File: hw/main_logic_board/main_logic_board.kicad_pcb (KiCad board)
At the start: 2 copper layers, 8 parts, among them J1 BATT_IN, J2 PWR_SEL, U1 PocketBeagle, U2 MPU-9250, U3 BME280

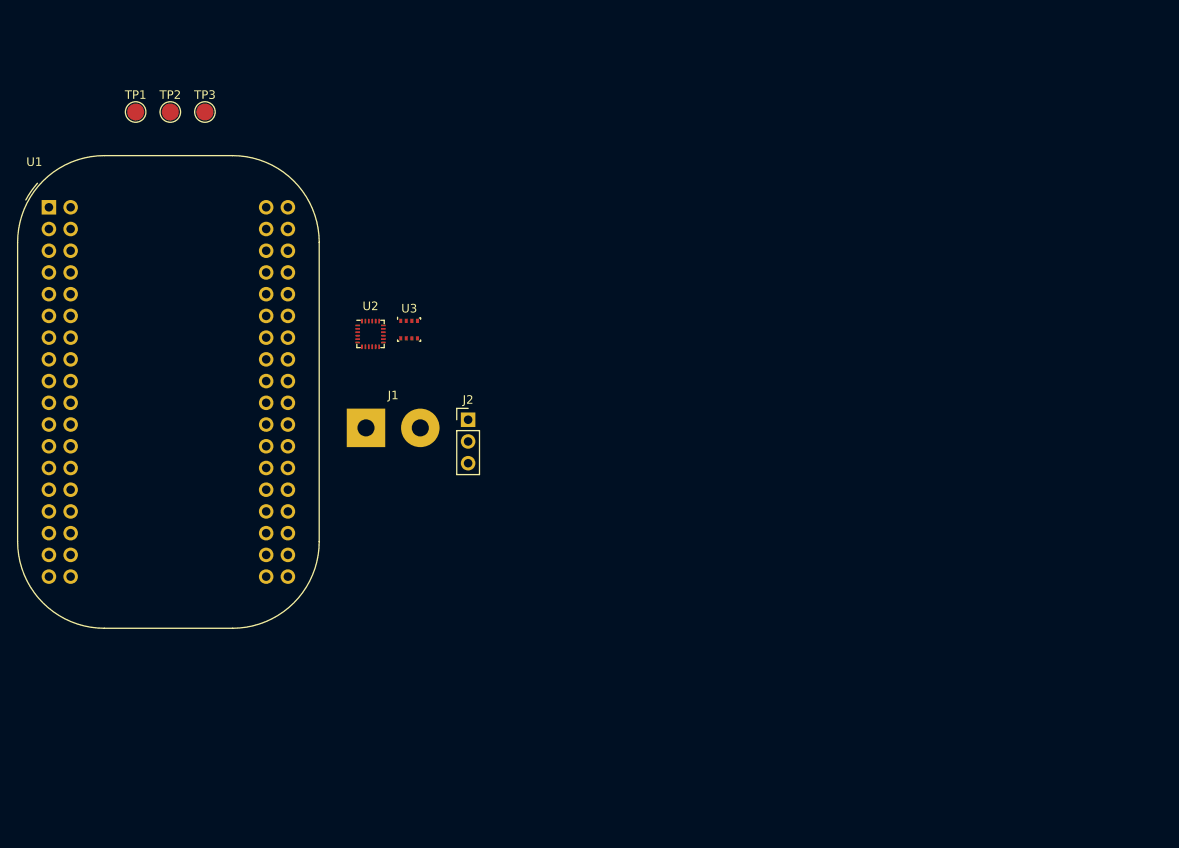
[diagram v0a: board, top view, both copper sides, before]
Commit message: Finish initial power schematics, swap some footprints for visualization in pcb view
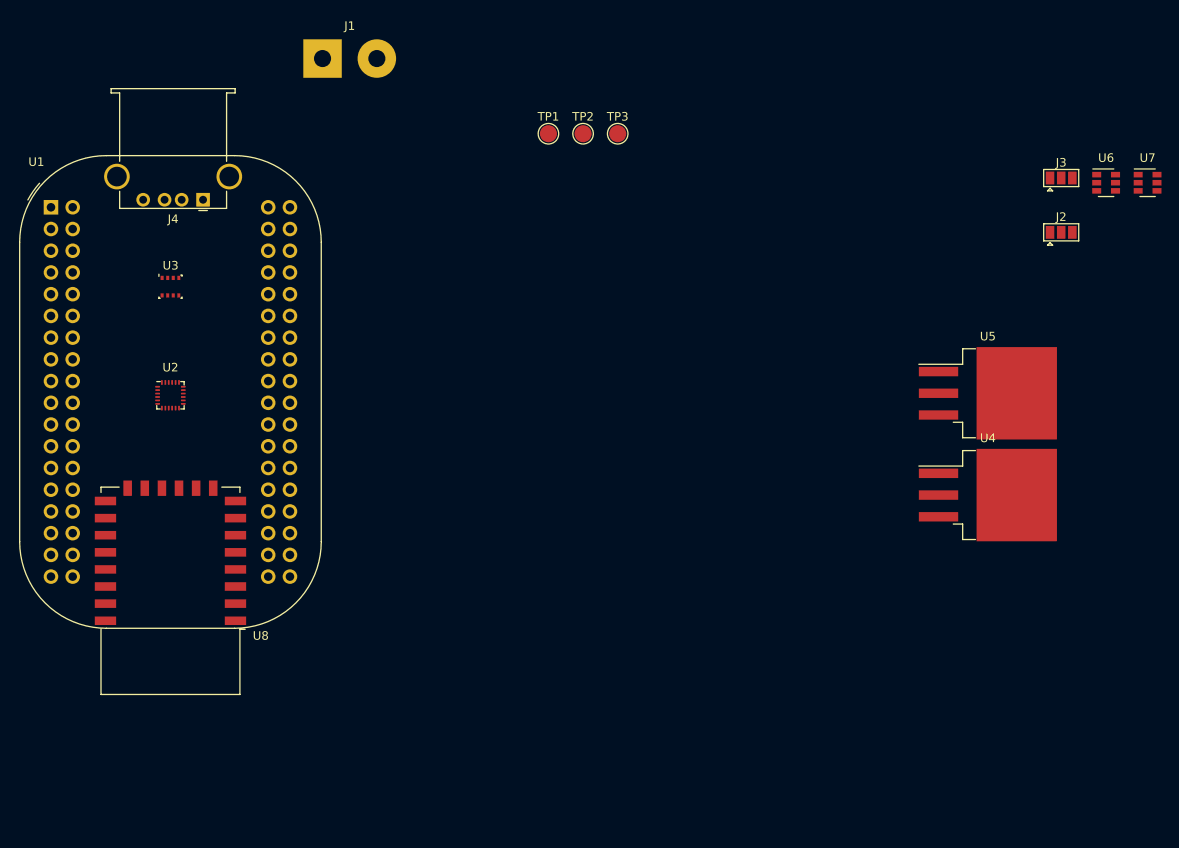
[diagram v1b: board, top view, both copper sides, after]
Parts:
- added J3: 3V3_PWR_SEL, Jumper:SolderJumper-3_P1.3mm_Open_Pad1.0x1.5mm, F.Cu at (221.0, 58.4)
- added J4: USB_A, Connector_USB:USB_A_Stewart_SS-52100-001_Horizontal, F.Cu at (120.7, 61.0)
- added U4: LM1085-5.0, Package_TO_SOT_SMD:TO-263-3_TabPin2, F.Cu at (212.4, 95.5)
- added U5: LM1085-3.3, Package_TO_SOT_SMD:TO-263-3_TabPin2, F.Cu at (212.4, 83.6)
- added U6: TPS563200, Package_TO_SOT_SMD:SOT-23-6, F.Cu at (226.2, 59.0)
- added U7: TPS563200, Package_TO_SOT_SMD:SOT-23-6, F.Cu at (231.1, 59.0)
- added U8: ESP-12F, RF_Module:ESP-12E, F.Cu at (116.8, 106.7)
- J2: value PWR_SEL -> 5V_PWR_SEL; footprint Connector_PinHeader_2.54mm:PinHeader_1x03_P2.54mm_Vertical -> Jumper:SolderJumper-3_P1.3mm_Open_Pad1.0x1.5mm
- moved J2 72.7 mm to (221.0, 64.8)
- moved TP2 48.3 mm to (165.1, 53.2)
- moved TP1 48.3 mm to (161.0, 53.2)
- moved TP3 48.3 mm to (169.1, 53.2)
- moved J1 43.5 mm to (134.6, 44.5)
- moved U3 28.3 mm to (116.8, 71.1)
- moved U2 24.5 mm to (116.8, 83.8)
- moved U1 0.24 mm to (102.9, 61.8)
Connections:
- net /RC_OUT_1 renamed /RC_OUT_5
- net Net-(U1-Pad19) renamed /AIN_1V8
- net Net-(U1-Pad20) renamed /GPIO20
- net Net-(U1-Pad34) renamed /GPIO26
- net Net-(U1-Pad36) renamed /PWM0
- net Net-(U1-Pad37) renamed /PWM1
- net Net-(U1-Pad39) renamed /GPIO23
- net Net-(U1-Pad55) renamed /GPIO27
- net Net-(U1-Pad64) renamed /RC_OUT_6
- net Net-(U1-Pad70) renamed /RC_OUT_4
- net Net-(U1-Pad71) renamed /AIN_3V3
- net Net-(U3-Pad4) renamed /SPI1_SCLK
- J1 pad 2: Net-(J1-Pad2) -> Net-(F1-Pad2)
- J2 pad 2: Net-(J1-Pad2) -> Net-(F1-Pad1)
- U1 pad 31: /RC_OUT_3 -> /RC_OUT_2
- U1 pad 33: /RC_OUT_0 -> /RC_OUT_3
- U1 pad 66: /RC_OUT_2 -> /SPI1_CS1
- U1 pad 67: /SPI1_CS -> /SPI1_CS0
- U2 pad 1: Net-(U2-Pad1) -> +3V3
- U2 pad 11: Net-(U2-Pad11) -> GND
- U2 pad 13: Net-(U2-Pad13) -> +3V3
- U2 pad 18: Net-(U2-Pad18) -> GND
- U2 pad 20: Net-(U2-Pad20) -> GND
- U2 pad 22: Net-(U2-Pad22) -> /SPI1_CS1
- U2 pad 23: Net-(U2-Pad23) -> /SPI1_CLK
- U2 pad 24: Net-(U2-Pad24) -> /SPI1_MOSI
- U2 pad 8: Net-(U2-Pad8) -> +3V3
- U2 pad 9: Net-(U2-Pad9) -> /SPI1_MISO
- U3 pad 1: Net-(U3-Pad1) -> GND
- U3 pad 2: Net-(U3-Pad2) -> /SPI1_CS0
- U3 pad 3: Net-(U3-Pad3) -> /SPI1_MOSI
- U3 pad 5: Net-(U3-Pad5) -> /SPI1_MISO
- U3 pad 6: Net-(U3-Pad6) -> +3V3
- U3 pad 7: Net-(U3-Pad7) -> GND
- U3 pad 8: Net-(U3-Pad8) -> +3V3

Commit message: Finish prelim schematic + PCB component placement
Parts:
- added C1: 47uF, Capacitor_SMD:C_0805_2012Metric, B.Cu at (142.4, 75.7)
- added C10: 10u, Capacitor_SMD:C_0805_2012Metric, B.Cu at (155.3, 98.4)
- added C11: 10u, Capacitor_SMD:C_0805_2012Metric, B.Cu at (155.3, 103.5)
- added C12: 10u, Capacitor_SMD:C_0805_2012Metric, B.Cu at (153.1, 98.4)
- added C13: 100n, Capacitor_SMD:C_0805_2012Metric, B.Cu at (154.6, 92.1)
- added C14: 100n, Capacitor_SMD:C_0805_2012Metric, B.Cu at (155.6, 109.3)
- added C15: 22u, Capacitor_SMD:C_0805_2012Metric, B.Cu at (166.6, 95.8)
- added C16: 22u, Capacitor_SMD:C_0805_2012Metric, B.Cu at (166.1, 105.8)
- added C17: 22u, Capacitor_SMD:C_0805_2012Metric, B.Cu at (168.8, 95.8)
- added C18: 22u, Capacitor_SMD:C_0805_2012Metric, B.Cu at (168.3, 105.8)
- added C19: 22u, Capacitor_SMD:C_0805_2012Metric, B.Cu at (170.6, 105.8)
- added C2: 10u, Capacitor_SMD:C_0805_2012Metric, B.Cu at (129.6, 96.7)
- added C20: 100n, Capacitor_SMD:C_0805_2012Metric, F.Cu at (151.8, 95.7)
- added C21: 100n, Capacitor_SMD:C_0805_2012Metric, F.Cu at (144.8, 95.7)
- added C22: 100n, Capacitor_SMD:C_0805_2012Metric, B.Cu at (152.3, 74.1)
- added C23: 10uF, Capacitor_SMD:C_0805_2012Metric, F.Cu at (143.8, 121.2)
- added C3: 10u, Capacitor_SMD:C_0805_2012Metric, B.Cu at (140.8, 93.9)
- added C4: 100n, Capacitor_SMD:C_0805_2012Metric, F.Cu at (151.8, 103.5)
- added C5: 100n, Capacitor_SMD:C_0805_2012Metric, F.Cu at (145.6, 88.2)
- added C6: 100n, Capacitor_SMD:C_0805_2012Metric, F.Cu at (145.1, 103.6)
- added C7: 10u, Capacitor_SMD:C_0805_2012Metric, B.Cu at (129.6, 102.9)
- added C8: 10u, Capacitor_SMD:C_0805_2012Metric, B.Cu at (140.8, 106.0)
- added C9: 10u, Capacitor_SMD:C_0805_2012Metric, B.Cu at (153.1, 103.5)
- added D1: WS2813, LED_SMD:LED_WS2812_PLCC6_5.0x5.0mm_P1.6mm, B.Cu at (135.1, 130.3)
- added D2: WS2813, LED_SMD:LED_WS2812_PLCC6_5.0x5.0mm_P1.6mm, B.Cu at (161.4, 130.3)
- added D3: WS2813, LED_SMD:LED_WS2812_PLCC6_5.0x5.0mm_P1.6mm, B.Cu at (161.2, 70.0)
- added D4: WS2813, LED_SMD:LED_WS2812_PLCC6_5.0x5.0mm_P1.6mm, B.Cu at (135.2, 70.0)
- added D5: RED, Diode_SMD:D_0805_2012Metric, F.Cu at (150.8, 130.6)
- added H1: GND, MountingHole:MountingHole_2.2mm_M2_Pad_Via, F.Cu at (126.6, 81.7)
- added H10: PWR, MountingHole:MountingHole_2.2mm_M2_Pad_Via, F.Cu at (174.3, 111.5)
- added H11: SIG, MountingHole:MountingHole_2.2mm_M2_Pad_Via, F.Cu at (174.0, 116.3)
- added H12: GND, MountingHole:MountingHole_2.2mm_M2_Pad_Via, F.Cu at (169.8, 118.7)
- added H2: SIG, MountingHole:MountingHole_2.2mm_M2_Pad_Via, F.Cu at (122.4, 84.1)
- added H3: PWR, MountingHole:MountingHole_2.2mm_M2_Pad_Via, F.Cu at (122.1, 88.9)
- added H4: PWR, MountingHole:MountingHole_2.2mm_M2_Pad_Via, F.Cu at (122.1, 111.5)
- added H5: SIG, MountingHole:MountingHole_2.2mm_M2_Pad_Via, F.Cu at (122.4, 116.3)
- added H6: GND, MountingHole:MountingHole_2.2mm_M2_Pad_Via, F.Cu at (126.6, 118.7)
- added H7: GND, MountingHole:MountingHole_2.2mm_M2_Pad_Via, F.Cu at (169.8, 81.7)
- added H8: SIG, MountingHole:MountingHole_2.2mm_M2_Pad_Via, F.Cu at (174.0, 84.1)
- added H9: PWR, MountingHole:MountingHole_2.2mm_M2_Pad_Via, F.Cu at (174.3, 88.9)
- added J10: RC_OUT_6, Connector_PinHeader_1.27mm:PinHeader_1x03_P1.27mm_Vertical, F.Cu at (150.0, 114.4)
- added J5: RC_OUT_1, Connector_PinHeader_1.27mm:PinHeader_1x03_P1.27mm_Vertical, F.Cu at (136.9, 75.5)
- added J6: RC_OUT_2, Connector_PinHeader_1.27mm:PinHeader_1x03_P1.27mm_Vertical, F.Cu at (134.3, 124.8)
- added J7: RC_OUT_3, Connector_PinHeader_1.27mm:PinHeader_1x03_P1.27mm_Vertical, F.Cu at (160.1, 75.5)
- added J8: RC_OUT_4, Connector_PinHeader_1.27mm:PinHeader_1x03_P1.27mm_Vertical, F.Cu at (160.0, 124.8)
- added J9: RC_OUT_5, Connector_PinHeader_1.27mm:PinHeader_1x03_P1.27mm_Vertical, F.Cu at (147.0, 114.4)
- added L1: 3.3u 20mOhm, Inductor_SMD:L_Abracon_ASPI-0630LR, B.Cu at (160.9, 90.3)
- added L2: 2.2u 15mOhm, Inductor_SMD:L_Vishay_IHLP-2020, B.Cu at (161.1, 110.5)
- added R1: 56.2k, Resistor_SMD:R_0805_2012Metric, B.Cu at (166.8, 90.3)
- added R10: 10K, Resistor_SMD:R_0805_2012Metric, F.Cu at (141.9, 126.8)
- added R2: 10k, Resistor_SMD:R_0805_2012Metric, B.Cu at (163.1, 96.0)
- added R3: 33.2k, Resistor_SMD:R_0805_2012Metric, B.Cu at (166.1, 110.7)
- added R4: 10k, Resistor_SMD:R_0805_2012Metric, B.Cu at (162.6, 105.5)
- added R5: 0R, Resistor_SMD:R_0805_2012Metric, F.Cu at (153.1, 74.3)
- added R6: 10K, Resistor_SMD:R_0805_2012Metric, F.Cu at (144.6, 131.3)
- added R7: 1K, Resistor_SMD:R_0805_2012Metric, F.Cu at (152.0, 125.6)
- added R8: 10K, Resistor_SMD:R_0805_2012Metric, F.Cu at (152.0, 123.4)
- added R9: 10K, Resistor_SMD:R_0805_2012Metric, F.Cu at (152.0, 121.2)
- added SW1: ESP_RESET, Button_Switch_SMD:SW_SPST_B3U-1000P, F.Cu at (141.8, 130.5)
- added SW2: ESP_GPIO0, Button_Switch_SMD:SW_SPST_B3U-1000P, F.Cu at (155.2, 130.5)
- added TP4: AIN_VREF+, TestPoint:TestPoint_Pad_D1.0mm, F.Cu at (141.2, 99.0)
- added TP5: AIN_VREF-, TestPoint:TestPoint_Pad_D1.0mm, F.Cu at (141.1, 102.0)
- added U10: ICM-20948, Sensor_Motion:InvenSense_QFN-24_3x3mm_P0.4mm, F.Cu at (148.3, 95.7)
- added U11: VL53L1X, Sensor_Distance:ST_VL53L1x, B.Cu at (148.5, 74.2)
- added U9: USBLC6-2P6, lib:SOT50P160X60-6N, F.Cu at (148.4, 75.0)
- J1: footprint Connector_Wire:SolderWirePad_1x02_P7.62mm_Drill2mm -> Connector_Wire:SolderWirePad_1x02_P5.08mm_Drill1.5mm
- J2, J3, U6, U7, U8: moved to B.Cu
- TP1: value TP_5V -> TP_5V_VIN; footprint TestPoint:TestPoint_Pad_D2.0mm -> TestPoint:TestPoint_Pad_D1.0mm
- TP2: value TP_3V3 -> TP_3V3_PB; footprint TestPoint:TestPoint_Pad_D2.0mm -> TestPoint:TestPoint_Pad_D1.0mm
- TP3: footprint TestPoint:TestPoint_Pad_D2.0mm -> TestPoint:TestPoint_Pad_D1.0mm
- U1: footprint Module:BeagleBoard_PocketBeagle -> lib:BeagleBoard_PocketBeagle_SMD
- U4: value LM1085-5.0 -> NCP1117-5.0_SOT223; footprint Package_TO_SOT_SMD:TO-263-3_TabPin2 -> Package_TO_SOT_SMD:SOT-223-3_TabPin2; moved to B.Cu
- U5: value LM1085-3.3 -> NCP1117-3.3_SOT223; footprint Package_TO_SOT_SMD:TO-263-3_TabPin2 -> Package_TO_SOT_SMD:SOT-223-3_TabPin2; moved to B.Cu
- moved J2 103.8 mm to (125.8, 106.1), turned to 180 degrees
- moved J3 101.5 mm to (125.8, 93.7)
- moved U7 86.0 mm to (158.7, 105.3)
- moved U5 80.0 mm to (135.2, 104.2)
- moved U4 77.3 mm to (135.2, 95.7)
- moved U6 77.2 mm to (158.7, 96.2)
- moved TP3 60.2 mm to (141.2, 106.5)
- moved J1 58.6 mm to (125.7, 102.4), turned to 90 degrees
- moved TP2 54.2 mm to (155.7, 106.7)
- moved U8 39.3 mm to (148.5, 130.0), turned to 0 degrees
- moved U2 37.3 mm to (148.4, 103.5)
- moved TP1 36.3 mm to (141.3, 83.8)
- moved U3 35.9 mm to (148.4, 88.2)
- moved U1 35.8 mm to (134.5, 78.6)
- moved J4 32.7 mm to (151.9, 70.7)
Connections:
- net /AIN_1V8 renamed /AIN_1V8_0
- net Net-(F1-Pad1) renamed +BATT
- net Net-(U1-Pad21) renamed /AIN_1V8_1
- net Net-(U8-Pad10) renamed /telemetry/TELEM_MISO
- net Net-(U8-Pad13) renamed /telemetry/TELEM_MOSI
- net Net-(U8-Pad14) renamed /telemetry/TELEM_SCLK
- net Net-(U8-Pad9) renamed /telemetry/TELEM_CS_N
- J4 pad 4: Net-(J4-Pad4) -> GND
- J4 pad 5: Net-(J4-Pad5) -> GND
- TP2 pad 1: +3V3 -> /3V3_PB
- U1 pad 13: Net-(U1-Pad13) -> GND
- U1 pad 14: +3V3 -> /3V3_PB
- U1 pad 26: /I2C_SDA -> /I2C2_SDA
- U1 pad 28: /I2C_SCL -> /I2C2_SCL
- U1 pad 29: Net-(U1-Pad29) -> /RC_OUT_1
- U1 pad 45: Net-(U1-Pad45) -> /I2C1_SCL
- U1 pad 47: Net-(U1-Pad47) -> /I2C1_SDA
- U1 pad 5: Net-(U1-Pad5) -> +5V
- U1 pad 59: +3V3 -> /3V3_PB
- U2 pad 22: /SPI1_CS1 -> /sensors/MPU_CS_N
- U2 pad 23: /SPI1_CLK -> /I2C2_SCL
- U2 pad 24: /SPI1_MOSI -> /I2C2_SDA
- U2 pad 9: /SPI1_MISO -> /sensors/MPU_MISO
- U3 pad 2: /SPI1_CS0 -> /sensors/BME_CS_N
- U3 pad 3: /SPI1_MOSI -> /I2C2_SDA
- U3 pad 4: /SPI1_SCLK -> /I2C2_SCL
- U3 pad 5: /SPI1_MISO -> /sensors/BME_MISO
- U8 pad 1: Net-(U8-Pad1) -> /telemetry/RST_N
- U8 pad 15: Net-(U8-Pad15) -> GND
- U8 pad 16: Net-(U8-Pad16) -> /telemetry/GPIO15
- U8 pad 17: Net-(U8-Pad17) -> /telemetry/GPIO2
- U8 pad 18: Net-(U8-Pad18) -> /telemetry/GPIO0
- U8 pad 21: Net-(U8-Pad21) -> /UART4_TX
- U8 pad 22: Net-(U8-Pad22) -> /UART4_RX
- U8 pad 3: Net-(U8-Pad3) -> /telemetry/CH_PD
- U8 pad 8: Net-(U8-Pad8) -> +3V3
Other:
- board outline added: 61.9 x 69 mm

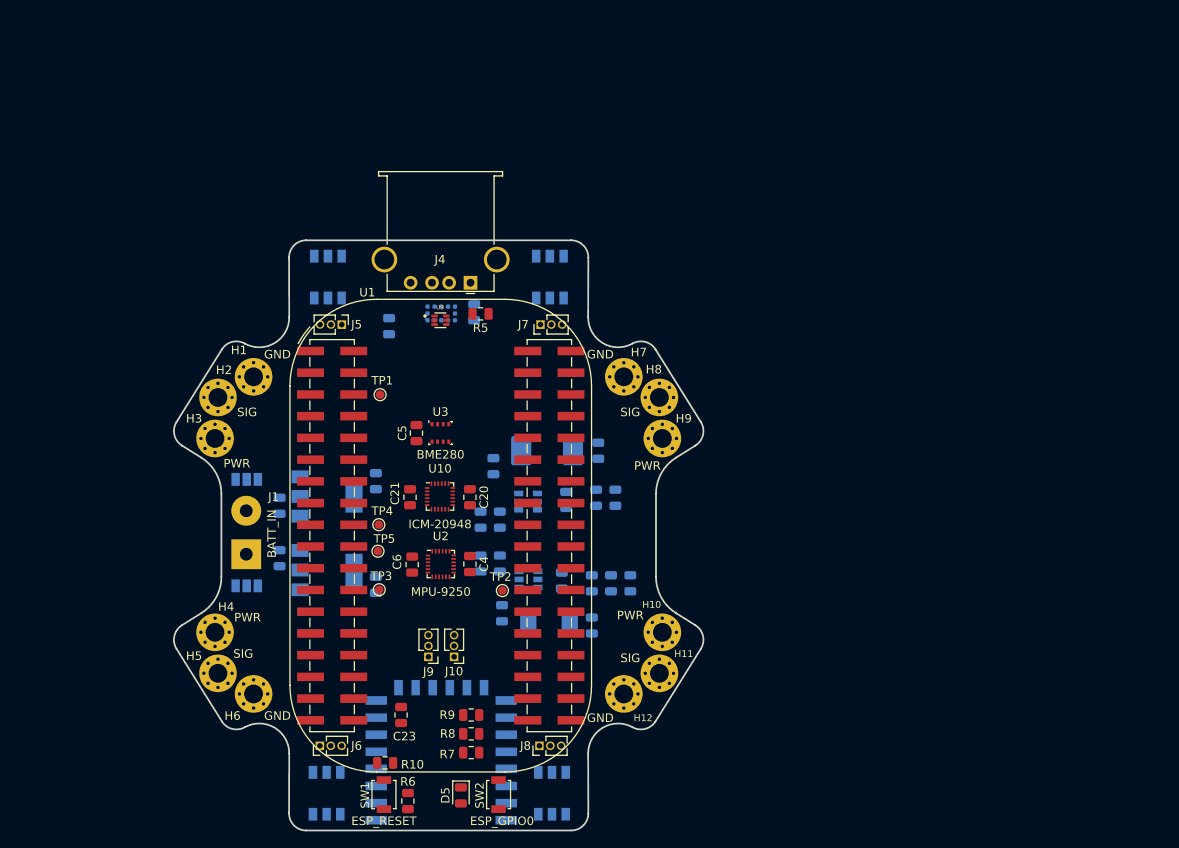
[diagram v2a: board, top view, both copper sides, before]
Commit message: Add debug headers, LED wiring, remove MPU
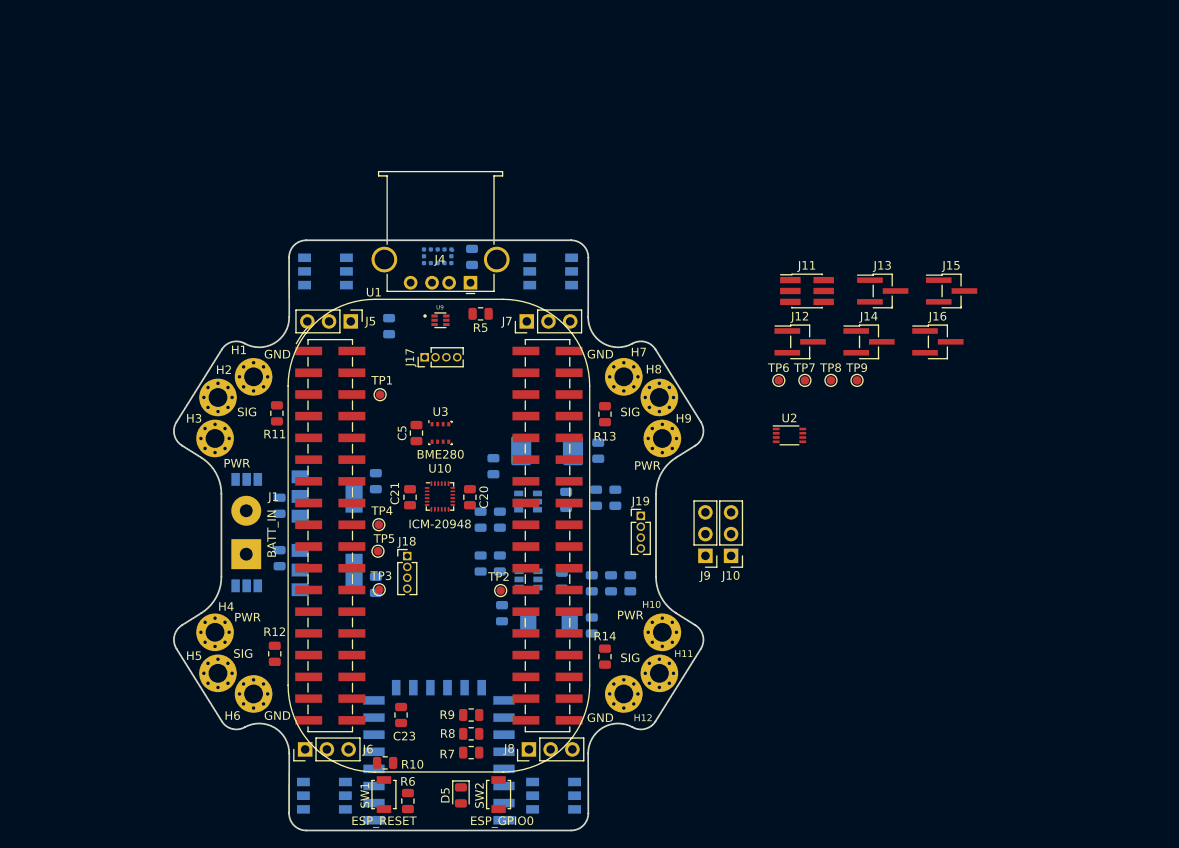
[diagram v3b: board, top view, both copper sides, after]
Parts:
- removed C4, C6: 100n, Capacitor_SMD:C_0805_2012Metric
- added J11: SPI1, Connector_PinHeader_1.27mm:PinHeader_2x03_P1.27mm_Vertical_SMD, F.Cu at (191.3, 71.6)
- added J12: UART0, Connector_PinHeader_1.27mm:PinHeader_1x03_P1.27mm_Vertical_SMD_Pin1Left, F.Cu at (190.5, 77.6)
- added J13: UART2, Connector_PinHeader_1.27mm:PinHeader_1x03_P1.27mm_Vertical_SMD_Pin1Left, F.Cu at (200.1, 71.6)
- added J14: UART4, Connector_PinHeader_1.27mm:PinHeader_1x03_P1.27mm_Vertical_SMD_Pin1Left, F.Cu at (198.5, 77.6)
- added J15: I2C1, Connector_PinHeader_1.27mm:PinHeader_1x03_P1.27mm_Vertical_SMD_Pin1Left, F.Cu at (208.2, 71.6)
- added J16: I2C2, Connector_PinHeader_1.27mm:PinHeader_1x03_P1.27mm_Vertical_SMD_Pin1Left, F.Cu at (206.6, 77.6)
- added J17: 5V, Connector_PinHeader_1.27mm:PinHeader_1x04_P1.27mm_Vertical, F.Cu at (146.6, 79.4)
- added J18: 3V3, Connector_PinHeader_1.27mm:PinHeader_1x04_P1.27mm_Vertical, F.Cu at (144.5, 102.6)
- added J19: BATT_V, Connector_PinHeader_1.27mm:PinHeader_1x04_P1.27mm_Vertical, F.Cu at (171.8, 97.9)
- added R11: 0R, Resistor_SMD:R_0805_2012Metric, F.Cu at (129.3, 85.9)
- added R12: 0R, Resistor_SMD:R_0805_2012Metric, F.Cu at (129.0, 114.0)
- added R13: 0R, Resistor_SMD:R_0805_2012Metric, F.Cu at (167.6, 86.0)
- added R14: 0R, Resistor_SMD:R_0805_2012Metric, F.Cu at (167.6, 114.4)
- added TP6: AIN_1, TestPoint:TestPoint_Pad_D1.0mm, F.Cu at (188.0, 82.1)
- added TP7: SPI1_CS1, TestPoint:TestPoint_Pad_D1.0mm, F.Cu at (191.0, 82.1)
- added TP8: RC_IN, TestPoint:TestPoint_Pad_D1.0mm, F.Cu at (194.1, 82.1)
- added TP9: AIN_0, TestPoint:TestPoint_Pad_D1.0mm, F.Cu at (197.1, 82.1)
- J10, J5, J6, J7, J8, J9: footprint Connector_PinHeader_1.27mm:PinHeader_1x03_P1.27mm_Vertical -> Connector_PinHeader_2.54mm:PinHeader_1x03_P2.54mm_Vertical
- U2: value MPU-9250 -> 74LVC2T45DC; footprint Sensor_Motion:InvenSense_QFN-24_3x3mm_P0.4mm -> Package_SO:VSSOP-8_2.3x2mm_P0.5mm
- moved D2 61.0 mm to (161.3, 69.3), turned to 0 degrees
- moved D1 61.0 mm to (135.0, 69.3), turned to 180 degrees
- moved D3 60.6 mm to (161.6, 130.6), turned to 180 degrees
- moved D4 60.6 mm to (134.8, 130.6), turned to 0 degrees
- moved U2 43.4 mm to (189.2, 88.5)
- moved J10 34.5 mm to (182.4, 102.6)
- moved J9 34.5 mm to (179.4, 102.6)
- moved U11 6.70 mm to (148.1, 67.6), turned to 180 degrees
- moved C22 6.47 mm to (152.1, 67.6)
- moved J6 1.77 mm to (132.6, 125.2)
- moved J7 1.65 mm to (158.5, 75.2)
- moved J8 1.30 mm to (158.8, 125.2)
- moved J5 1.11 mm to (137.9, 75.2)
- moved U8 0.27 mm to (148.2, 130.0)
- moved U1 0.22 mm to (134.3, 78.6)
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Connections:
- net Net-(D4-Pad3) renamed /actuation/LED_DATA_OUT
- net Net-(U1-Pad35) renamed /LED_DATA
- D1 pad 2: Net-(D1-Pad2) -> +5V
- D1 pad 5: Net-(D1-Pad5) -> GND
- D2 pad 2: Net-(D2-Pad2) -> +5V
- D2 pad 4: Net-(D2-Pad4) -> Net-(D1-Pad3)
- D2 pad 5: Net-(D2-Pad5) -> GND
- D3 pad 2: Net-(D3-Pad2) -> +5V
- D3 pad 4: Net-(D3-Pad4) -> Net-(D2-Pad3)
- D3 pad 5: Net-(D3-Pad5) -> GND
- D4 pad 2: Net-(D4-Pad2) -> +5V
- D4 pad 4: Net-(D4-Pad4) -> Net-(D3-Pad3)
- D4 pad 5: Net-(D4-Pad5) -> GND
- H11 pad 1: /RC_OUT_4 -> Net-(H11-Pad1)
- H2 pad 1: /RC_OUT_1 -> Net-(H2-Pad1)
- H5 pad 1: /RC_OUT_2 -> Net-(H5-Pad1)
- H8 pad 1: /RC_OUT_3 -> Net-(H8-Pad1)
- U1 pad 54: Net-(U1-Pad54) -> /RC_IN
- U2 pad 2: (no net) -> /actuation/LED_DATA_IN
- U2 pad 3: (no net) -> Net-(U2-Pad3)
- U2 pad 4: (no net) -> GND
- U2 pad 5: (no net) -> +3V3
- U2 pad 6: (no net) -> Net-(U2-Pad6)
- U2 pad 7: Net-(U2-Pad7) -> Net-(D1-Pad4)
- U2 pad 8: +3V3 -> +5V
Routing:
- added copper zone on PWR.Cu, net +3V3
- added copper zone on PWR.Cu, net +BATT
- added copper zone on GND.Cu, net GND
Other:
- copper layers 2 -> 4
